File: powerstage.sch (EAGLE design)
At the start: 42 parts, among them CON1 PINHEAD_1X10-2-FEMALE, CON2 BATTERY_CON-2P-XT30-RA, CON3 PINHEAD_1X10-2-FEMALE, IC5 MCP9700, Q1 BUK9K6R2-40E,115, Q2 BUK9K6R2-40E,115, Q3 BUK9K6R2-40E,115

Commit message: 1210 ceramic capacitors replaced with better ones
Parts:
- C31, C35, C58, C62, C63, C64: device C_digikey:10µF-50V_20%_X5R-C1210 -> C_digikey:10µF-50_10%_X7S-C1210
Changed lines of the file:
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@@
 </attributes>
 <variantdefs>
-<variantdef name="BASIC" current="yes"/>
+<variantdef name="BASIC"/>
 </variantdefs>
 <classes>
@@
 <variant name="BASIC" populate="no"/>
 </part>
-<part name="C35" library="C_digikey" library_urn="urn:adsk.eagle:library:2539367" deviceset="10µF" device="-C1210" package3d_urn="urn:adsk.eagle:package:2539380/2" technology="-50V_20%_X5R" value="10µF"/>
-<part name="C58" library="C_digikey" library_urn="urn:adsk.eagle:library:2539367" deviceset="10µF" device="-C1210" package3d_urn="urn:adsk.eagle:package:2539380/2" technology="-50V_20%_X5R" value="10µF"/>
-<part name="C62" library="C_digikey" library_urn="urn:adsk.eagle:library:2539367" deviceset="10µF" device="-C1210" package3d_urn="urn:adsk.eagle:package:2539380/2" technology="-50V_20%_X5R" value="10µF"/>
-<part name="C63" library="C_digikey" library_urn="urn:adsk.eagle:library:2539367" deviceset="10µF" device="-C1210" package3d_urn="urn:adsk.eagle:package:2539380/2" technology="-50V_20%_X5R" value="10µF"/>
-<part name="C64" library="C_digikey" library_urn="urn:adsk.eagle:library:2539367" deviceset="10µF" device="-C1210" package3d_urn="urn:adsk.eagle:package:2539380/2" technology="-50V_20%_X5R" value="10µF"/>
-<part name="C31" library="C_digikey" library_urn="urn:adsk.eagle:library:2539367" deviceset="10µF" device="-C1210" package3d_urn="urn:adsk.eagle:package:2539380/2" technology="-50V_20%_X5R" value="10µF"/>
+<part name="C35" library="C_digikey" library_urn="urn:adsk.eagle:library:2539367" deviceset="10µF" device="-C1210" package3d_urn="urn:adsk.eagle:package:2539380/2" technology="-50_10%_X7S" value="10µF"/>
+<part name="C58" library="C_digikey" library_urn="urn:adsk.eagle:library:2539367" deviceset="10µF" device="-C1210" package3d_urn="urn:adsk.eagle:package:2539380/2" technology="-50_10%_X7S" value="10µF"/>
+<part name="C62" library="C_digikey" library_urn="urn:adsk.eagle:library:2539367" deviceset="10µF" device="-C1210" package3d_urn="urn:adsk.eagle:package:2539380/2" technology="-50_10%_X7S" value="10µF"/>
+<part name="C63" library="C_digikey" library_urn="urn:adsk.eagle:library:2539367" deviceset="10µF" device="-C1210" package3d_urn="urn:adsk.eagle:package:2539380/2" technology="-50_10%_X7S" value="10µF"/>
+<part name="C64" library="C_digikey" library_urn="urn:adsk.eagle:library:2539367" deviceset="10µF" device="-C1210" package3d_urn="urn:adsk.eagle:package:2539380/2" technology="-50_10%_X7S" value="10µF"/>
+<part name="C31" library="C_digikey" library_urn="urn:adsk.eagle:library:2539367" deviceset="10µF" device="-C1210" package3d_urn="urn:adsk.eagle:package:2539380/2" technology="-50_10%_X7S" value="10µF"/>
 <part name="FRAME1" library="frames" library_urn="urn:adsk.eagle:library:229" deviceset="A3L-LOC" device=""/>
 <part name="GND2" library="supply_symbols" library_urn="urn:adsk.eagle:library:5017758" deviceset="PGND" device="" value="PGND"/>

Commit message: updated compnents naming. Updated production docs
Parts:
- removed C62, C63: 10µF, C_digikey:10µF-50_10%_X7S-C1210
- removed R15: 4R3, R_digikey:4R3-5%-0402
- removed R18: 3 mOhms, SHUNT_RESISTORS:CURRENT_SHUNT_KELVIN-0.003R-2512-KELVIN
- added C7: 0.1µF, C_digikey:0.1µF-16V_10%_X7R-0402
- added C8: 4.7µF, C_digikey:4.7µF-25V_10%_X6S-0603
- added R1: 3 mOhms, SHUNT_RESISTORS:CURRENT_SHUNT_KELVIN-0.003R-2512-KELVIN
- added R4: 4R3, R_digikey:4R3-5%-0402
- C13: value 0.1µF -> 10µF; device C_digikey:0.1µF-16V_10%_X7R-0402 -> C_digikey:10µF-50_10%_X7S-C1210
- C14: value 4.7µF -> 10µF; device C_digikey:4.7µF-25V_10%_X6S-0603 -> C_digikey:10µF-50_10%_X7S-C1210
- CON2: value BATTERY_CON-2P-XT30-RA -> PINHEAD_1X10-2-FEMALE; device Connectors:BATTERY_CON-2P-XT30-RA -> pinhead:PINHEAD_1X10-2-FEMALE
- CON3: value PINHEAD_1X10-2-FEMALE -> BATTERY_CON-2P-XT30-RA; device pinhead:PINHEAD_1X10-2-FEMALE -> Connectors:BATTERY_CON-2P-XT30-RA
- R2: value 4R3 -> 3 mOhms; device R_digikey:4R3-5%-0402 -> SHUNT_RESISTORS:CURRENT_SHUNT_KELVIN-0.003R-2512-KELVIN
- R5: value 3 mOhms -> 4R3; device SHUNT_RESISTORS:CURRENT_SHUNT_KELVIN-0.003R-2512-KELVIN -> R_digikey:4R3-5%-0402
- renumbered C31 to C10, C35 to C11, C58 to C12, C64 to C15, IC5 to IC1, R16 to R6, R22 to R7, R23 to R8, R27 to R9
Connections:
- net N$1: now also R3.2; no longer R2.2
- net N$10: now also C8.2; no longer C14.2
- net N$2: now also R4.2; no longer R3.2
- net N$3: now also R5.2; no longer R15.2
- net PGND: now also C7.1, C8.1, CON2.10, CON3.-, CON3.PAD1, CON3.PAD2, R1.2, R2.2; no longer C62.1, C63.1, CON2.-, CON2.PAD1, CON2.PAD2, CON3.10, R18.2, R5.2
- net PHASE_A: now also CON2.7; no longer CON3.7
- net PHASE_A_CURRENT_SHUNT_N: now also R1.S1; no longer R5.S1
- net PHASE_A_CURRENT_SHUNT_P: now also R1.S2; no longer R5.S2
- net PHASE_A_GATE_HIGH: now also CON2.8, R3.1; no longer CON3.8, R2.1
- net PHASE_A_GATE_LOW: now also CON2.6, R4.1; no longer CON3.6, R3.1
- net PHASE_A_GND: now also CON2.5, R1.1; no longer CON3.5, R5.1
- net PHASE_B_CURRENT_SHUNT_N: now also R2.S1; no longer R18.S1
- net PHASE_B_CURRENT_SHUNT_P: now also R2.S2; no longer R18.S2
- net PHASE_B_GATE_HIGH: now also R5.1; no longer R15.1
- net PHASE_B_GND: now also R2.1; no longer R18.1
- net PHASE_C: now also CON2.3; no longer CON3.3
- net PHASE_C_GATE_HIGH: now also CON2.4; no longer CON3.4
- net PHASE_C_GATE_LOW: now also CON2.2; no longer CON3.2
- net PHASE_C_GND: now also CON2.1; no longer CON3.1
- net TEMPERATURE_SENSOR: now also C7.2; no longer C13.2
- net VDC: now also C13.2, C14.2, CON2.9, CON3.+; no longer C62.2, C63.2, CON2.+, CON3.9
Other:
- moved on the sheet: C13, C14, R3

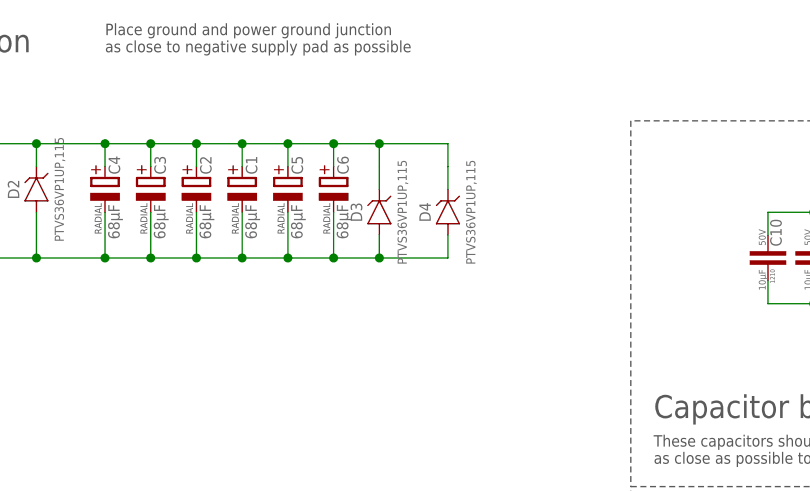
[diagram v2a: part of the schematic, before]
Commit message: let there be holes in powerstage as well
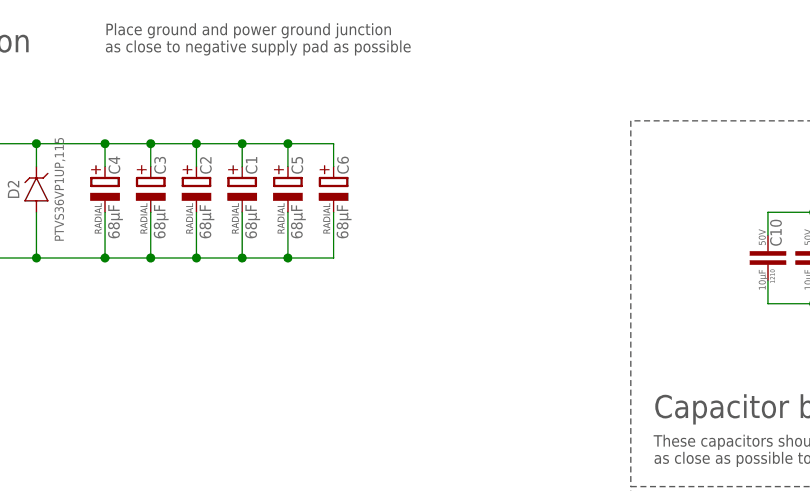
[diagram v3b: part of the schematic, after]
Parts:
- removed D3, D4: PTVS36VP1UP,115-36V-SOD128, TVS_diodes:PTVS36VP1UP,115-36V-SOD128
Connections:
- net PGND: no longer D3.A, D4.A
- net VDC: no longer D3.C, D4.C
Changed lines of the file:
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@@
 <?xml version="1.0" encoding="utf-8"?>
 <!DOCTYPE eagle SYSTEM "eagle.dtd">
-<eagle version="9.2.2">
+<eagle version="9.3.2">
 <drawing>
 <settings>
@@
 <part name="+P2" library="supply_symbols" library_urn="urn:adsk.eagle:library:5017758" deviceset="VDC" device=""/>
 <part name="GND5" library="supply_symbols" library_urn="urn:adsk.eagle:library:5017758" deviceset="PGND" device="" value="PGND"/>
-<part name="D3" library="TVS_diodes" library_urn="urn:adsk.eagle:library:3333632" deviceset="PTVS36VP1UP,115" device="-SOD128" package3d_urn="urn:adsk.eagle:package:6533206/2" technology="-36V">
-<variant name="BASIC" populate="no"/>
-</part>
-<part name="D4" library="TVS_diodes" library_urn="urn:adsk.eagle:library:3333632" deviceset="PTVS36VP1UP,115" device="-SOD128" package3d_urn="urn:adsk.eagle:package:6533206/2" technology="-36V">
-<variant name="BASIC" populate="no"/>
-</part>
 <part name="GND7" library="supply_symbols" library_urn="urn:adsk.eagle:library:5017758" deviceset="PGND" device="" value="PGND"/>
 <part name="U$8" library="usb2can_master_lib" deviceset="FIDUCIALMOUNT" device="">
@@
 <attribute name="VALUE" x="167.64" y="156.21" size="1.27" layer="97" font="vector" ratio="15" align="center"/>
 </instance>
-<instance part="D3" gate="G$1" x="109.22" y="226.06" smashed="yes" rot="R90">
-<attribute name="NAME" x="106.68" y="226.06" size="1.27" layer="95" font="vector" ratio="15" rot="R90" align="center"/>
-<attribute name="MANF#" x="111.76" y="226.06" size="1.016" layer="95" font="vector" ratio="15" rot="R90" align="center"/>
-</instance>
-<instance part="D4" gate="G$1" x="116.84" y="226.06" smashed="yes" rot="R90">
-<attribute name="NAME" x="114.3" y="226.06" size="1.27" layer="95" font="vector" ratio="15" rot="R90" align="center"/>
-<attribute name="MANF#" x="119.38" y="226.06" size="1.016" layer="95" font="vector" ratio="15" rot="R90" align="center"/>
-</instance>
 <instance part="GND7" gate="G$1" x="208.28" y="121.92" smashed="yes" rot="R90">
 <attribute name="VALUE" x="209.55" y="121.92" size="1.27" layer="97" font="vector" ratio="15" rot="R90" align="center"/>
@@
 <wire x1="45.72" y1="226.06" x2="45.72" y2="220.98" width="0.1524" layer="91"/>
 <wire x1="45.72" y1="220.98" x2="48.26" y2="220.98" width="0.1524" layer="91"/>
-<wire x1="104.14" y1="220.98" x2="109.22" y2="220.98" width="0.1524" layer="91"/>
-<junction x="104.14" y="220.98"/>
-<pinref part="D3" gate="G$1" pin="A"/>
-<wire x1="109.22" y1="220.98" x2="109.22" y2="223.52" width="0.1524" layer="91"/>
-<wire x1="109.22" y1="220.98" x2="116.84" y2="220.98" width="0.1524" layer="91"/>
-<junction x="109.22" y="220.98"/>
-<pinref part="D4" gate="G$1" pin="A"/>
-<wire x1="116.84" y1="220.98" x2="116.84" y2="223.52" width="0.1524" layer="91"/>
 <pinref part="CON3" gate="G$1" pin="PAD1"/>
 <wire x1="35.56" y1="223.52" x2="35.56" y2="220.98" width="0.1524" layer="91"/>
@@
 <wire x1="45.72" y1="228.6" x2="45.72" y2="233.68" width="0.1524" layer="91"/>
 <wire x1="45.72" y1="233.68" x2="48.26" y2="233.68" width="0.1524" layer="91"/>
-<wire x1="104.14" y1="233.68" x2="109.22" y2="233.68" width="0.1524" layer="91"/>
-<junction x="104.14" y="233.68"/>
-<pinref part="D3" gate="G$1" pin="C"/>
-<wire x1="109.22" y1="231.14" x2="109.22" y2="228.6" width="0.1524" layer="91"/>
-<pinref part="D4" gate="G$1" pin="C"/>
-<wire x1="116.84" y1="231.14" x2="116.84" y2="228.6" width="0.1524" layer="91"/>
-<wire x1="109.22" y1="233.68" x2="109.22" y2="231.14" width="0.1524" layer="91"/>
-<wire x1="109.22" y1="233.68" x2="116.84" y2="233.68" width="0.1524" layer="91"/>
-<junction x="109.22" y="233.68"/>
-<wire x1="116.84" y1="233.68" x2="116.84" y2="231.14" width="0.1524" layer="91"/>
-</segment>
-<segment>
+</segment>
+<segment>

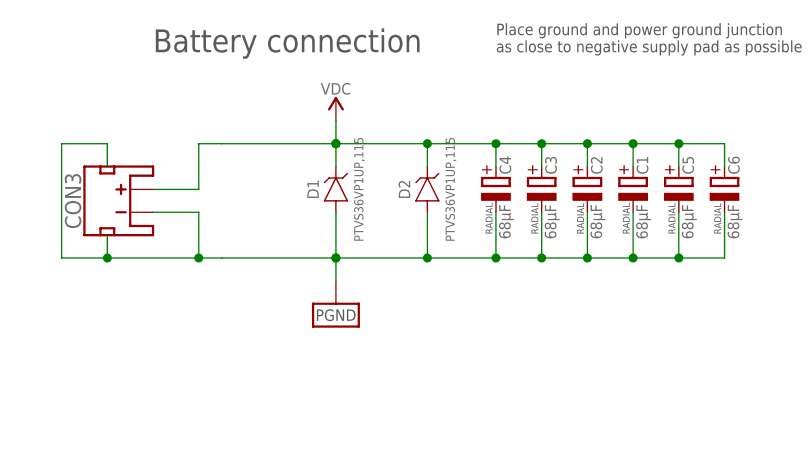
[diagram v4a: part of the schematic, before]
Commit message: TVS diode replaced
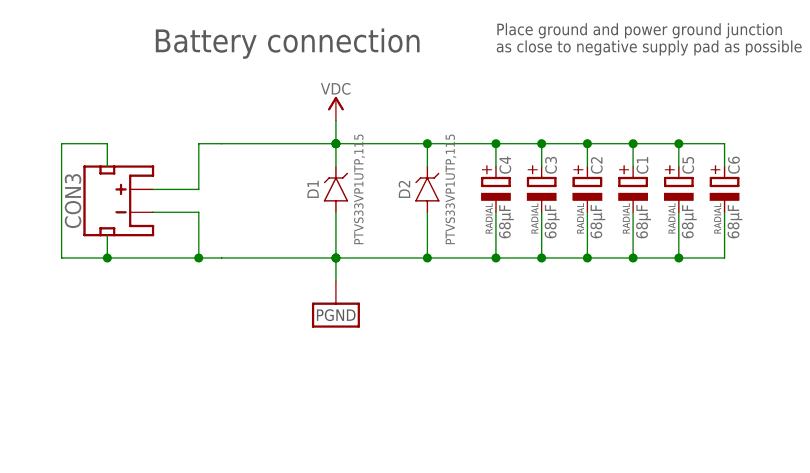
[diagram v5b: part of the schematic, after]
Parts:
- D1, D2: value PTVS36VP1UP,115-36V-SOD128 -> PTVS33VP1UTP,115-36V-SOD128; device TVS_diodes:PTVS36VP1UP,115-36V-SOD128 -> TVS_diodes:PTVS33VP1UTP,115-36V-SOD128
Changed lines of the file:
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@@
 <layer number="58" name="bCAD" color="9" fill="1" visible="no" active="no"/>
 <layer number="59" name="Invisible" color="7" fill="1" visible="no" active="no"/>
+<layer number="60" name="bCarbon" color="7" fill="1" visible="no" active="no"/>
 <layer number="61" name="stand" color="7" fill="1" visible="no" active="no"/>
 <layer number="88" name="SimResults" color="9" fill="1" visible="yes" active="yes"/>
@@
 <layer number="127" name="_tvalues" color="7" fill="1" visible="yes" active="yes"/>
 <layer number="128" name="_bvalues" color="7" fill="1" visible="yes" active="yes"/>
+<layer number="129" name="Mask" color="7" fill="1" visible="yes" active="yes"/>
 <layer number="130" name="bLogo" color="7" fill="1" visible="yes" active="yes"/>
 <layer number="131" name="tAdjust" color="7" fill="1" visible="yes" active="yes"/>
@@
 <attribute name="PACKAGE" value="RADIAL"/>
 </part>
-<part name="D1" library="TVS_diodes" library_urn="urn:adsk.eagle:library:3333632" deviceset="PTVS36VP1UP,115" device="-SOD128" package3d_urn="urn:adsk.eagle:package:6533206/2" technology="-36V"/>
-<part name="D2" library="TVS_diodes" library_urn="urn:adsk.eagle:library:3333632" deviceset="PTVS36VP1UP,115" device="-SOD128" package3d_urn="urn:adsk.eagle:package:6533206/2" technology="-36V"/>
+<part name="D1" library="TVS_diodes" library_urn="urn:adsk.eagle:library:3333632" deviceset="PTVS33VP1UTP,115" device="-SOD128" package3d_urn="urn:adsk.eagle:package:6533206/2" technology="-36V"/>
+<part name="D2" library="TVS_diodes" library_urn="urn:adsk.eagle:library:3333632" deviceset="PTVS33VP1UTP,115" device="-SOD128" package3d_urn="urn:adsk.eagle:package:6533206/2" technology="-36V"/>
 <part name="+P1" library="supply_symbols" library_urn="urn:adsk.eagle:library:5017758" deviceset="5V" device=""/>
 <part name="+P2" library="supply_symbols" library_urn="urn:adsk.eagle:library:5017758" deviceset="VDC" device=""/>

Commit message: updated attributes (#19)
added MANF and MANF# attributes to the connectors and powerstage schematics
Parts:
- C5, C6: MANF (none) -> Wurth Electronics Inc; MANF# (none) -> 860020673014
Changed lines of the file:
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@@
 <?xml version="1.0" encoding="utf-8"?>
 <!DOCTYPE eagle SYSTEM "eagle.dtd">
-<eagle version="9.3.2">
+<eagle version="9.6.2">
 <drawing>
 <settings>
@@
 <part name="C5" library="rc" library_urn="urn:adsk.eagle:library:2539423" deviceset="CPOL" device="-RADIAL_6.3X12.5" package3d_urn="urn:adsk.eagle:package:6513892/3" value="68µF">
 <attribute name="DIGIKEY#" value="732-8860-1-ND"/>
+<attribute name="MANF" value="Wurth Electronics Inc"/>
+<attribute name="MANF#" value="860020673014"/>
 <attribute name="PACKAGE" value="RADIAL"/>
 </part>
@@
 <part name="C6" library="rc" library_urn="urn:adsk.eagle:library:2539423" deviceset="CPOL" device="-RADIAL_6.3X12.5" package3d_urn="urn:adsk.eagle:package:6513892/3" value="68µF">
 <attribute name="DIGIKEY#" value="732-8860-1-ND"/>
+<attribute name="MANF" value="Wurth Electronics Inc"/>
+<attribute name="MANF#" value="860020673014"/>
 <attribute name="PACKAGE" value="RADIAL"/>
 </part>
@@
 <attribute name="PACKAGE" x="98.298" y="227.076" size="0.762" layer="97" font="vector" rot="R90" align="center-right"/>
 <attribute name="DIGIKEY#" x="99.06" y="228.6" size="1.778" layer="96" rot="R90" display="off"/>
+<attribute name="MANF" x="99.06" y="228.6" size="1.778" layer="96" rot="R90" display="off"/>
+<attribute name="MANF#" x="99.06" y="228.6" size="1.778" layer="96" rot="R90" display="off"/>
 </instance>
 <instance part="C2" gate="G$1" x="88.9" y="228.6" smashed="yes" rot="R90">
@@
 <attribute name="PACKAGE" x="103.378" y="227.076" size="0.762" layer="97" font="vector" rot="R90" align="center-right"/>
 <attribute name="DIGIKEY#" x="104.14" y="228.6" size="1.778" layer="96" rot="R90" display="off"/>
+<attribute name="MANF" x="104.14" y="228.6" size="1.778" layer="96" rot="R90" display="off"/>
+<attribute name="MANF#" x="104.14" y="228.6" size="1.778" layer="96" rot="R90" display="off"/>
 </instance>
 <instance part="D1" gate="G$1" x="60.96" y="228.6" smashed="yes" rot="R90">
